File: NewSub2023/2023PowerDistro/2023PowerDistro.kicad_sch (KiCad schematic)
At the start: 3 parts, among them U1 L7805

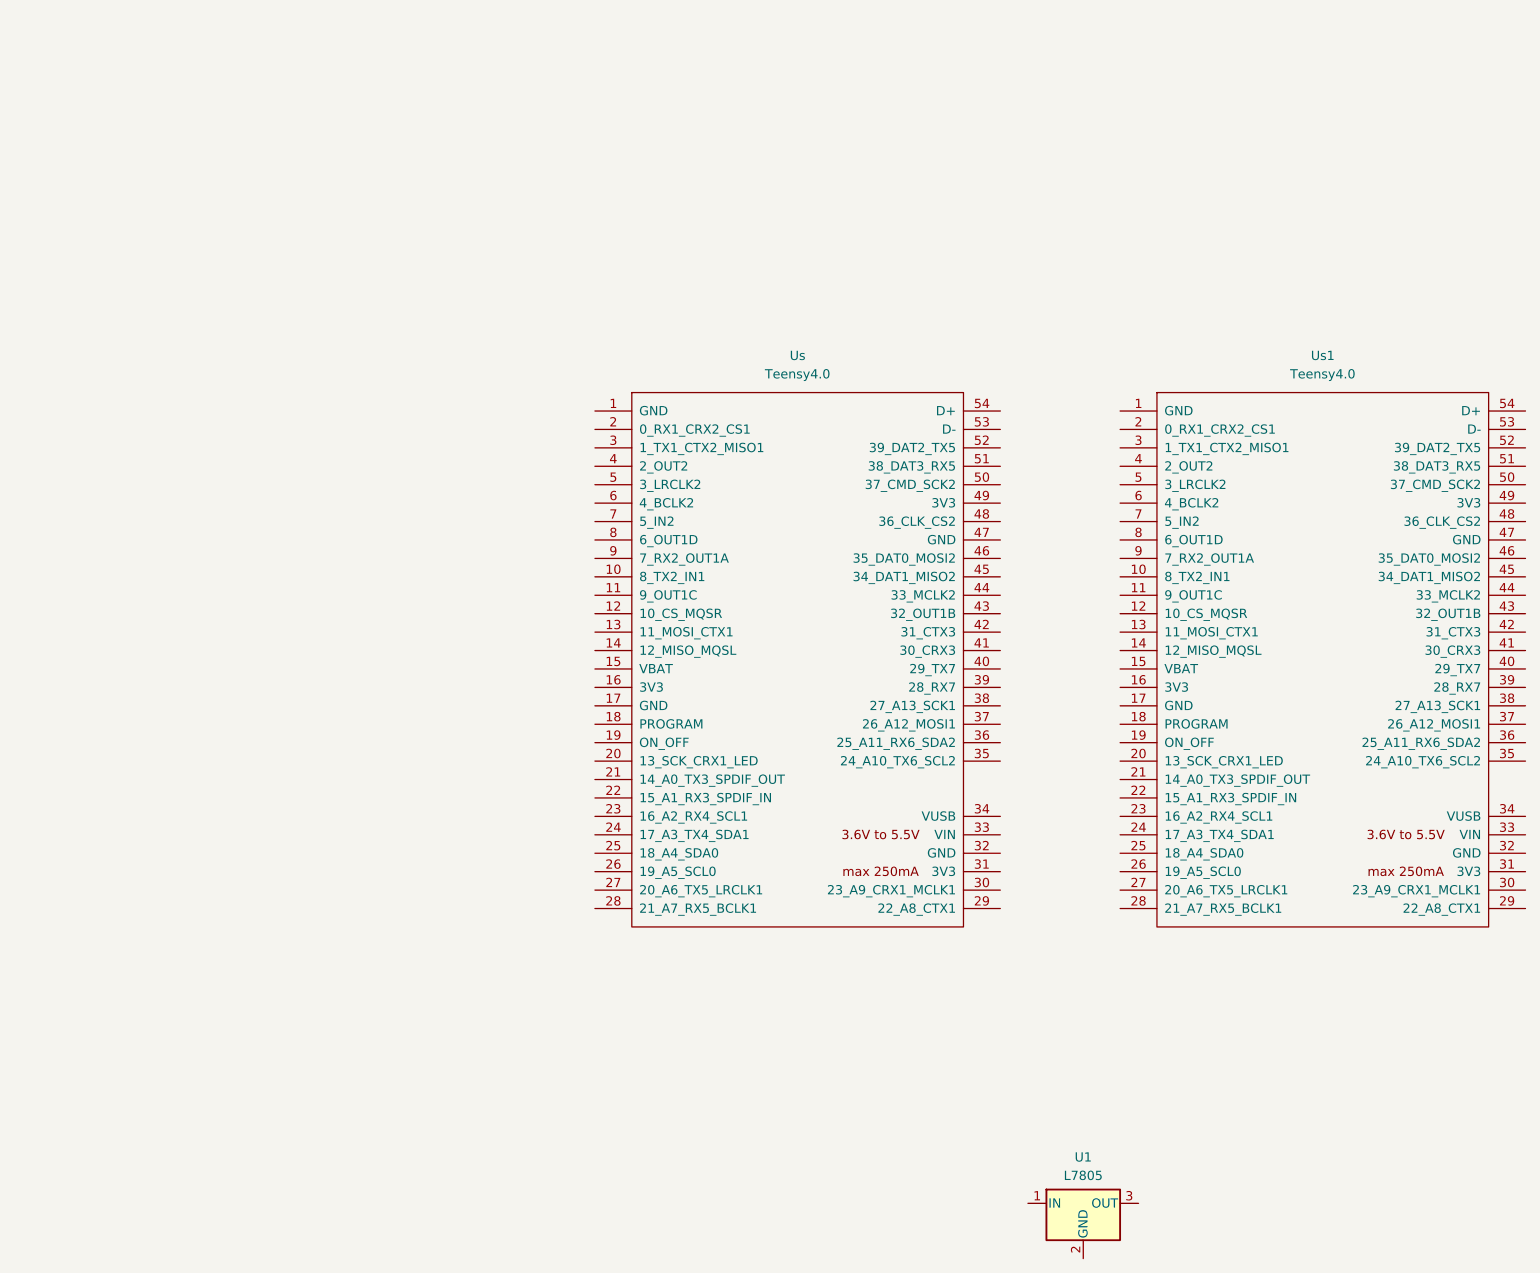
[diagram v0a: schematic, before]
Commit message: Added power block, teensy block, and 5v reg to schematic. Revised custom symbols.
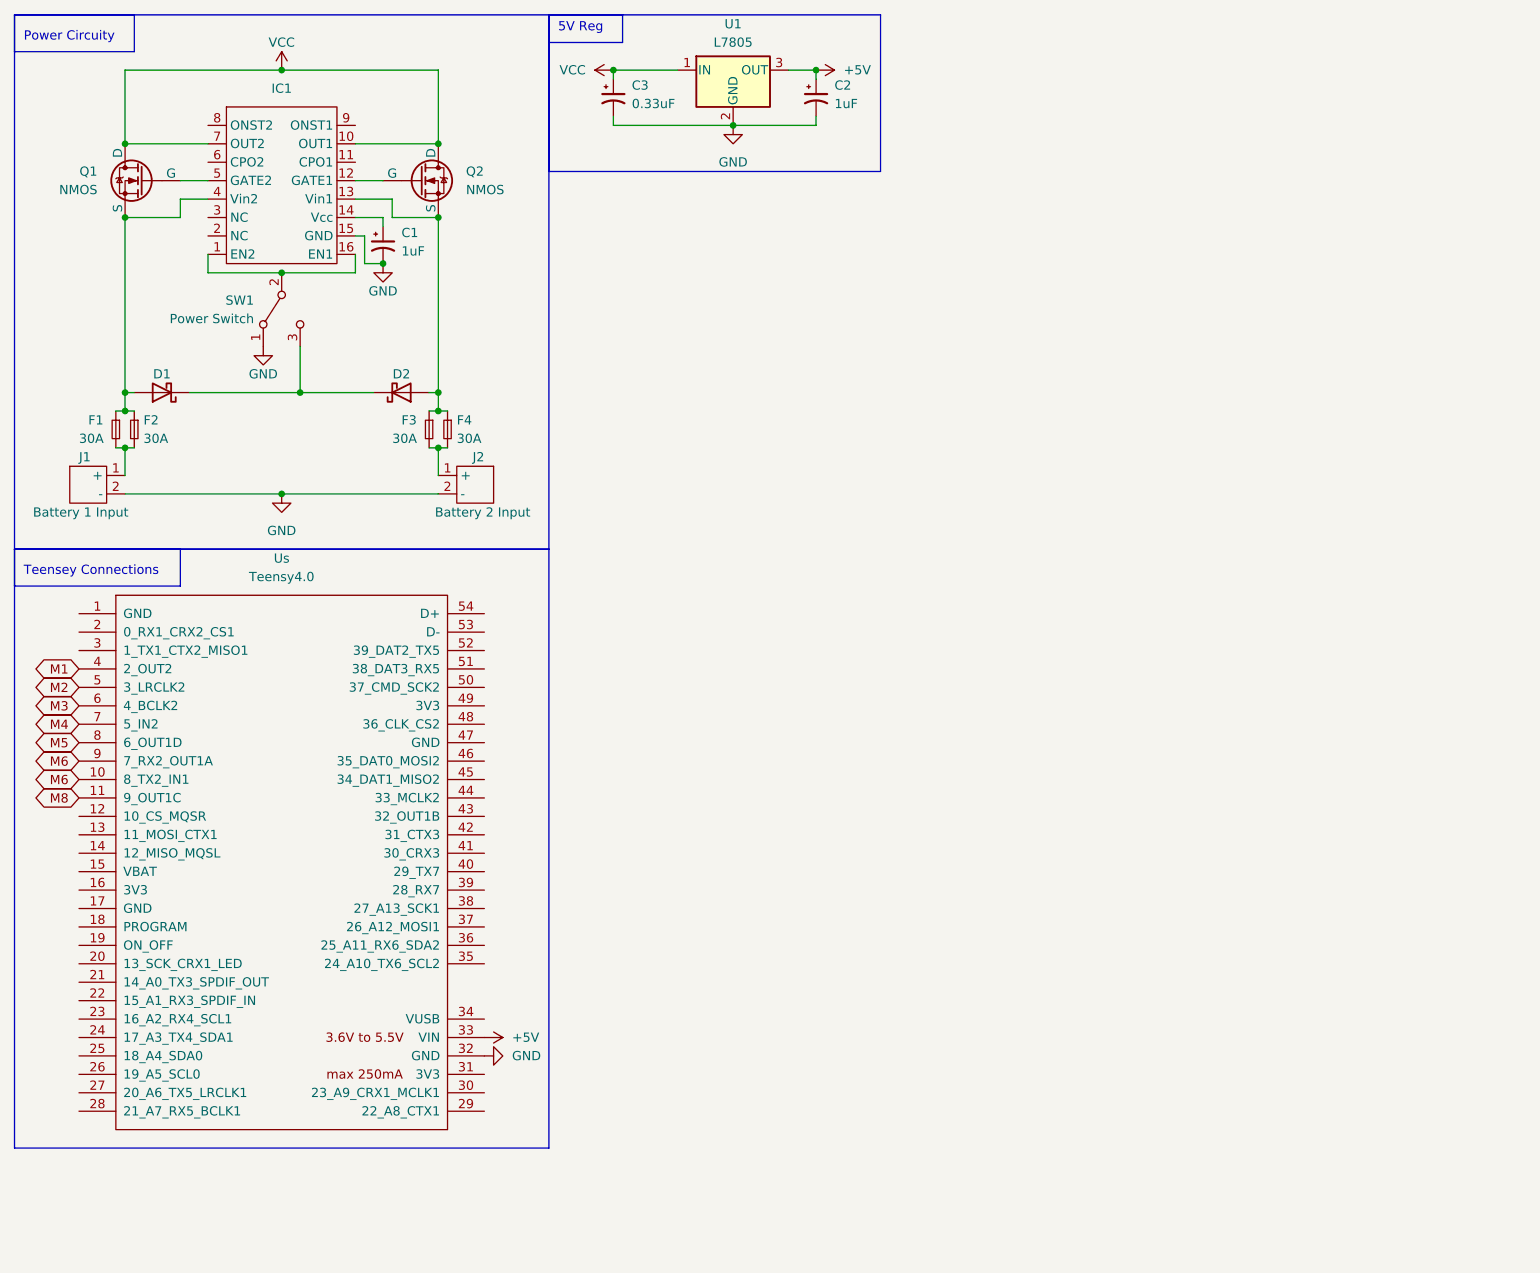
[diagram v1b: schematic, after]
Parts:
- removed Us1: Teensy4.0, symbol 2023Symbols:Teensy4.0
- added C1, C2: 1uF, symbol Device:C_Polarized_Small_US
- added C3: 0.33uF, symbol Device:C_Polarized_Small_US
- added D1, D2: ~, symbol Device:D_Schottky
- added F1, F2, F3, F4: 30A, symbol Device:Fuse_Small
- added IC1: ~, symbol 2023Symbols:LTC4353
- added J1: Battery 1 Input, symbol 2023Symbols:XT90PW-M
- added J2: Battery 2 Input, symbol 2023Symbols:XT90PW-M
- added Q1, Q2: NMOS, symbol Simulation_SPICE:NMOS
- added SW1: Power Switch, symbol Switch:SW_SPDT
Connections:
- net VCC: now reaches U1.1 (IN)
- net VCC: now also C3.1, IC1.10 (OUT1), IC1.7 (OUT2), Q1.1 (D), Q2.1 (D)
- net GND: now reaches U1.2 (GND)
- net GND: now also Us.32 (GND), C1.2, C2.2, C3.2, IC1.15 (GND), J1.2 (-), J2.2 (-), SW1.1 (A)
- net +5V: now reaches U1.3 (OUT)
- net +5V: now also Us.33 (VIN), C2.1
- net M6: now reaches Us.10 (8_TX2_IN1)
- net M6: now also Us.9 (7_RX2_OUT1A)
- net M8: now reaches Us.11 (9_OUT1C)
- net M1: now reaches Us.4 (2_OUT2)
- net M2: now reaches Us.5 (3_LRCLK2)
- net M3: now reaches Us.6 (4_BCLK2)
- net M4: now reaches Us.7 (5_IN2)
- net M5: now reaches Us.8 (6_OUT1D)
- new net: IC1.1 (EN2), IC1.16 (EN1), SW1.2 (B)
- new net: D1.1 (K), D2.1 (K), SW1.3 (C)
- new net: IC1.12 (GATE1), Q2.2 (G)
- new net: D2.2 (A), F3.1, F4.1, IC1.13 (Vin1), Q2.3 (S)
- new net: C1.1, IC1.14 (Vcc)
- new net: D1.2 (A), F1.1, F2.1, IC1.4 (Vin2), Q1.3 (S)
- new net: IC1.5 (GATE2), Q1.2 (G)
- new net: F3.2, F4.2, J2.1 (+)
- new net: F1.2, F2.2, J1.1 (+)
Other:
- note added: "5V Reg"
- note added: "Power Circuity"
- note added: "Teensey Connections"
- moved on the sheet: U1, Us
